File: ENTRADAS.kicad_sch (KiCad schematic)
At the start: 27 parts, among them IC14 ILD206T, IC15 ILD206T, IC16 ILD206T, J12 1728810000, J7 1728840000, U10 MAX3227

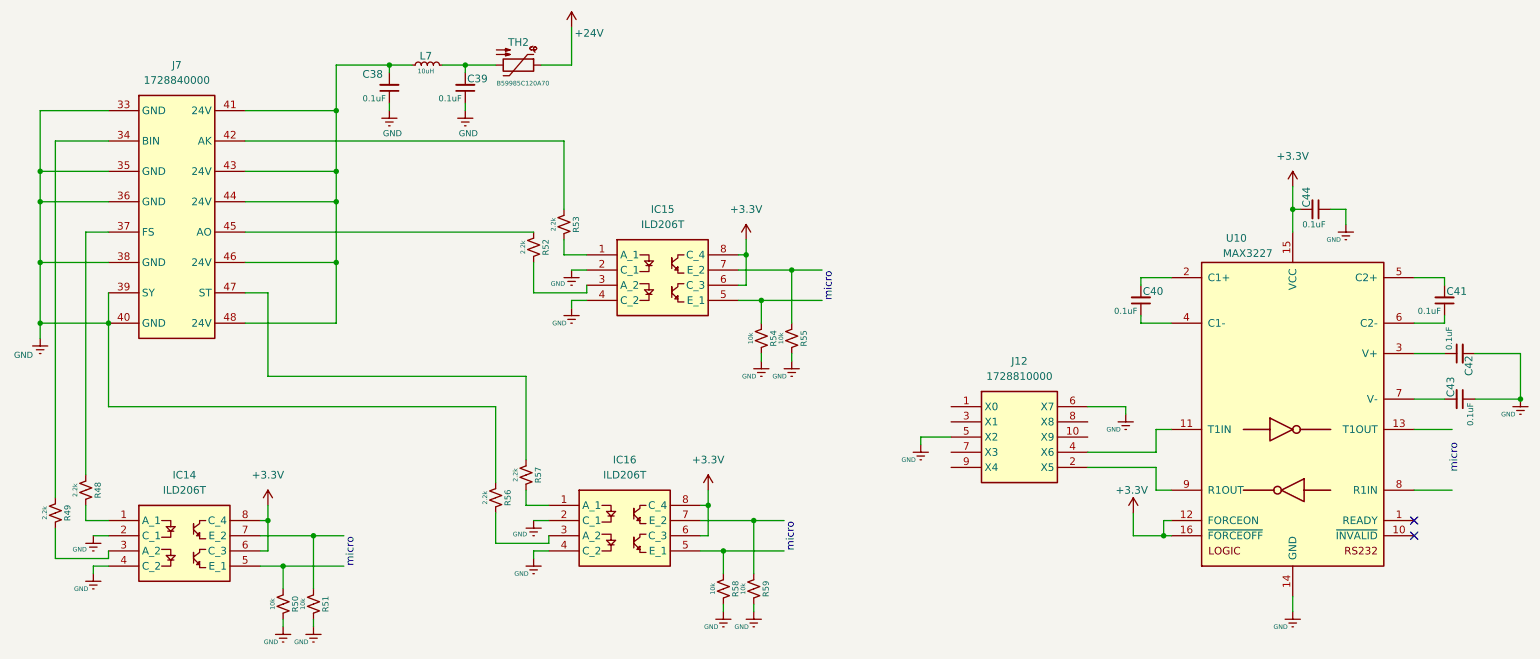
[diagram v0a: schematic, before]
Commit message: 7-may-26 346
se esta trabajando en los reles esquematico y pcb
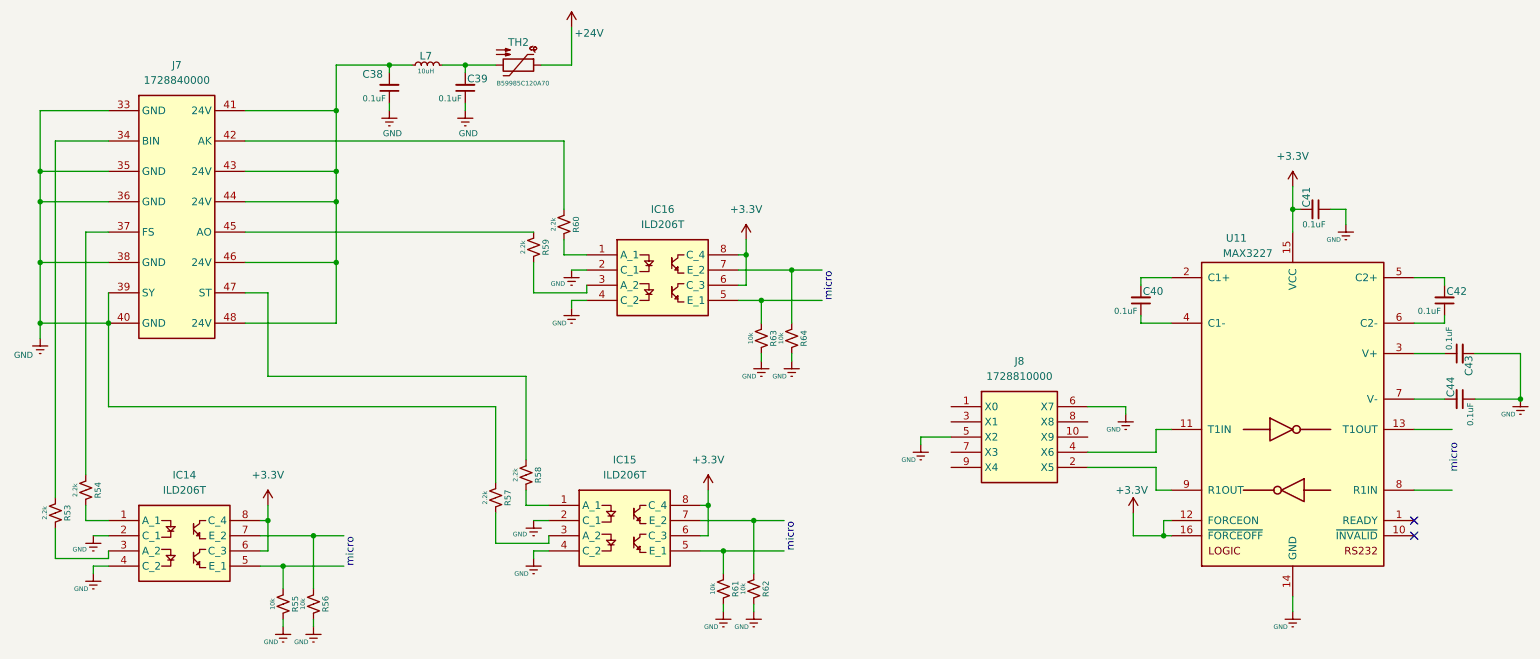
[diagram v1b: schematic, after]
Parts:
- renumbered C44 to C41, C41 to C42, C42 to C43, C43 to C44, IC16 to IC15, IC15 to IC16, J12 to J8, R49 to R53, R48 to R54, R50 to R55, R51 to R56, R56 to R57, R57 to R58, R52 to R59, R53 to R60, R58 to R61, R59 to R62, R54 to R63, R55 to R64, U10 to U11
